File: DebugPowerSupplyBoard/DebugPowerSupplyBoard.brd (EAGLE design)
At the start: 160 x 100 mm, 281 parts, among them IC1 LD117AV33, IC2 7805T

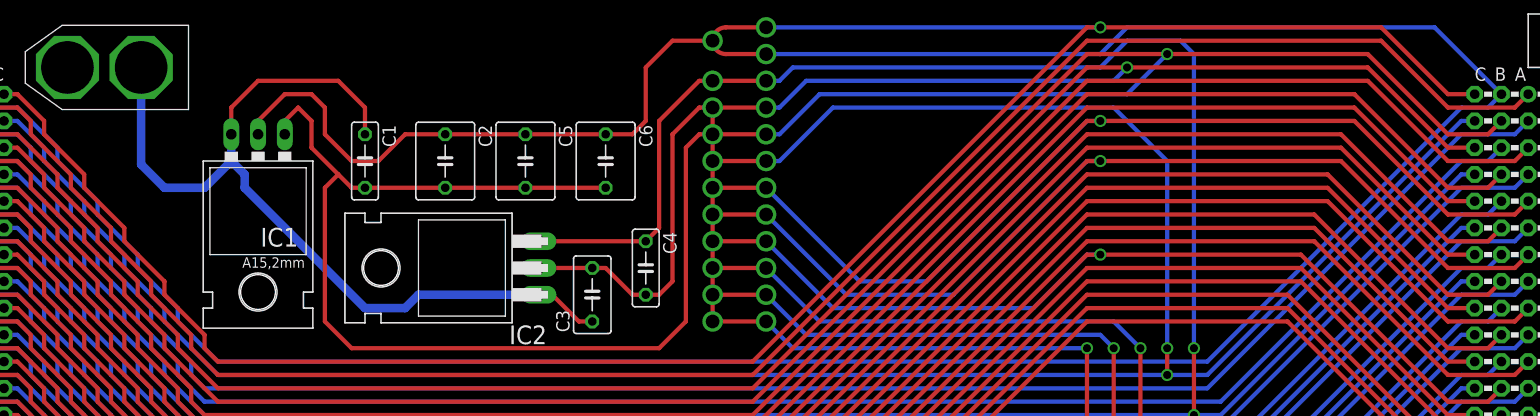
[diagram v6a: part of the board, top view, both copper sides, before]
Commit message: All the grounds have the same name now, so Eagle knows to connect them.
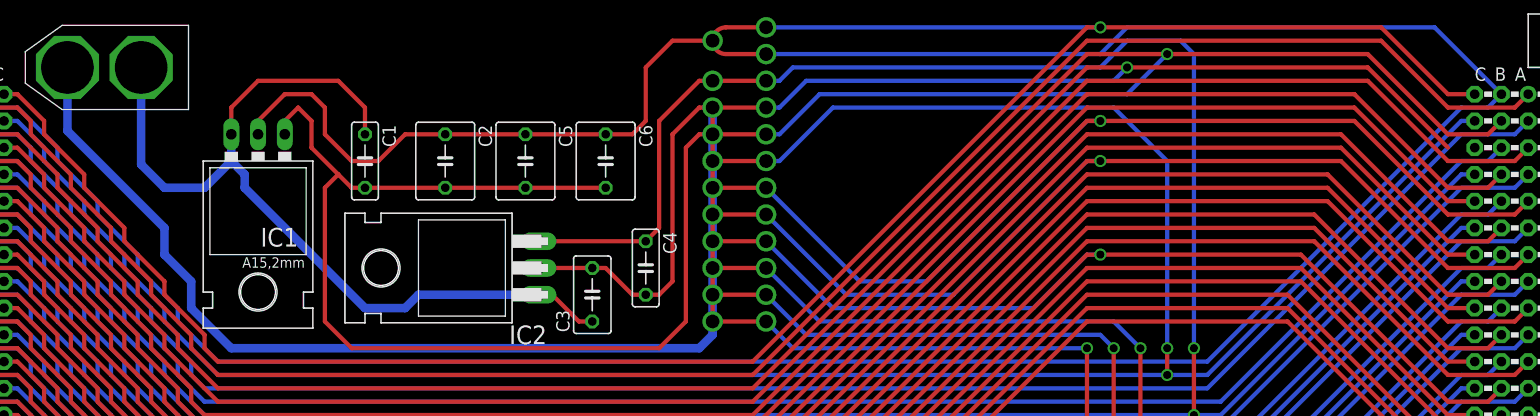
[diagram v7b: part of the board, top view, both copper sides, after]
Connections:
- removed net GND_3V3: C1.2, C2.2, C5.2, C6.2, IC1.1, J1.B2, J1.C2, J2.B2, J2.C2
- removed net GND_5V: C3.2, C4.2, IC2.2, J1.C3, J2.C3
- net GND: now also C1.2, C2.2, C3.2, C4.2, C5.2, C6.2, IC1.1, IC2.2, J1.B2, J1.C2, J1.C3, J2.B2, J2.C2, J2.C3
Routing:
- net GND: track 1353.4 -> 2259.2 mm, vias 21 -> 31
- net GND_3V3: track 564.3 -> 0.00 mm, vias 7 -> 0
- net GND_5V: track 243.0 -> 0.00 mm, vias 3 -> 0

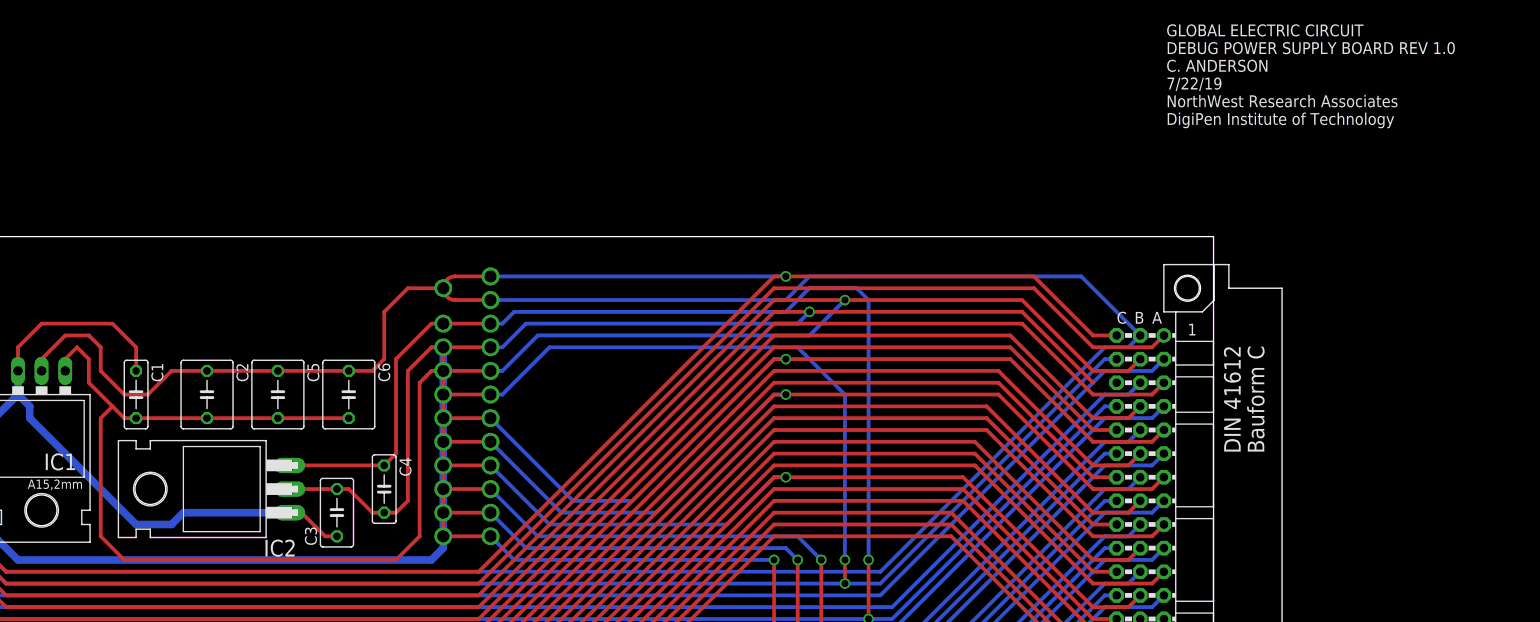
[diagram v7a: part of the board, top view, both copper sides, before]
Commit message: Labeled all the GND etc. pins and applied the decal
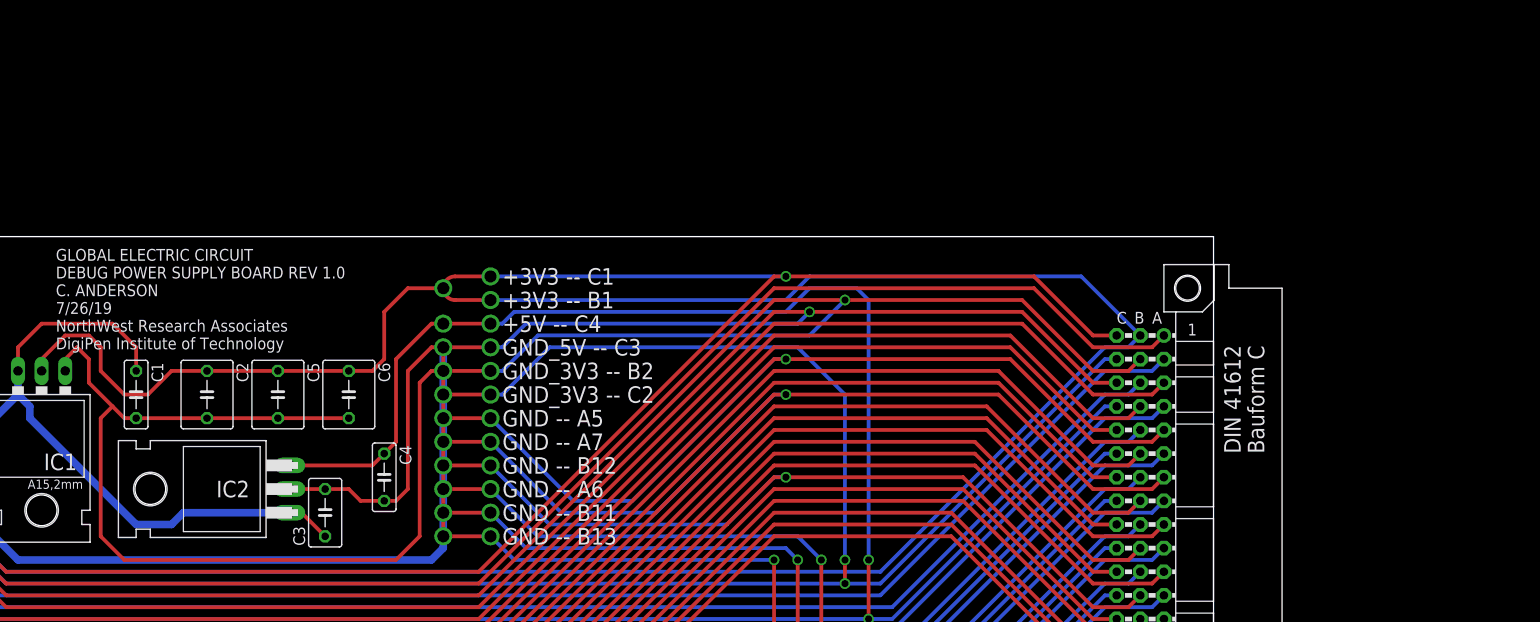
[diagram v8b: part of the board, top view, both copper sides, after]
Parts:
- moved U$249 301.4 mm to (137.2, 78.7), turned to 180 degrees
- moved U$255 298.8 mm to (134.6, 83.8), turned to 180 degrees
- moved U$250 297.6 mm to (134.6, 81.3), turned to 180 degrees
- moved U$248 296.4 mm to (134.6, 78.7), turned to 180 degrees
- moved U$246 295.4 mm to (134.6, 76.2), turned to 180 degrees
- moved U$247 294.4 mm to (134.6, 73.7), turned to 180 degrees
- moved U$254 293.9 mm to (132.1, 83.8), turned to 180 degrees
- moved U$251 292.6 mm to (132.1, 81.3), turned to 180 degrees
- moved U$245 290.4 mm to (132.1, 76.2), turned to 180 degrees
- moved U$244 289.4 mm to (132.1, 73.7), turned to 180 degrees
- moved U$253 288.9 mm to (129.5, 83.8), turned to 180 degrees
- moved U$252 287.7 mm to (129.5, 81.3), turned to 180 degrees
- moved U$241 284.4 mm to (129.5, 73.7), turned to 180 degrees
- moved U$256 284.0 mm to (127.0, 83.8), turned to 180 degrees
- moved U$240 283.5 mm to (129.5, 71.1), turned to 180 degrees
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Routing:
- net VIN: track 84.6 -> 83.3 mm
- net +5V: track 272.5 -> 271.8 mm
- net GND: track 2259.2 -> 2259.9 mm
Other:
- board text added: "+3V3 -- B1"
- board text added: "+3V3 -- C1"
- board text added: "+5V -- C4"
- board text added: "GLOBAL ELECTRIC CIRCUIT DEBUG POWER SUPPLY BOARD REV 1.0 C. ANDERSON 7/26/19 NorthWest Research Associates DigiPen Institute of Technology"
- board text added: "GND -- A5"
- board text added: "GND -- A6"
- board text added: "GND -- A7"
- board text added: "GND -- B11"
- board text added: "GND -- B12"
- board text added: "GND -- B13"
- board text added: "GND_3V3 -- B2"
- board text added: "GND_3V3 -- C2"
- board text added: "GND_5V -- C3"
- board text removed: "GLOBAL ELECTRIC CIRCUIT DEBUG POWER SUPPLY BOARD REV 1.0 C. ANDERSON 7/22/19 NorthWest Research Associates DigiPen Institute of Technology"
